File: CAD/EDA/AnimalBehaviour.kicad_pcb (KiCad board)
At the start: 2 copper layers, 106 x 86 mm, 26 parts, among them J1 SSR_INPUT, J10 Cam, J11 Imaging, J12 JSolenoid, J13 StimIsoIN, J2 SSR OUT, J3 StimCurrentInject, J4 StimIsoIN, J5 Imaging, J6 CAM, J7 AudioJack2, J8 Ext Supp, J9 LED, Q1 IRF540N, U1 4N35

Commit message: temp commit.
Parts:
- R1, R2, R3, R4: footprint Resistor_THT:R_Axial_DIN0414_L11.9mm_D4.5mm_P25.40mm_Horizontal -> Resistor_THT:R_Axial_DIN0309_L9.0mm_D3.2mm_P5.08mm_Vertical
- moved J7 81.4 mm to (115.6, 105.4), turned to 90 degrees
- moved J9 54.4 mm to (119.4, 92.7), turned to 90 degrees
- moved RotaryEncoder1 37.2 mm to (191.1, 102.9), turned to 270 degrees
- moved R2 33.3 mm to (148.0, 113.0), turned to 180 degrees
- moved R3 25.5 mm to (138.4, 113.0)
- moved J10 25.4 mm to (175.9, 63.5)
- moved J11 24.7 mm to (149.2, 62.9)
- moved Q1 23.1 mm to (152.4, 97.2), turned to 90 degrees
- moved R1 20.7 mm to (138.4, 106.7)
- moved J1 19.1 mm to (120.0, 77.5), turned to 270 degrees
- moved R4 17.1 mm to (117.5, 97.2)
- moved J8 14.1 mm to (116.2, 132.7)
- moved J12 12.9 mm to (116.8, 118.7)
- moved C1 8.78 mm to (172.7, 111.2)
- moved U1 8.17 mm to (164.5, 112.4)
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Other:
- net class Default: clearance 0.4 -> 0.25
- rule trace_clearance: 0.4 -> 0.25

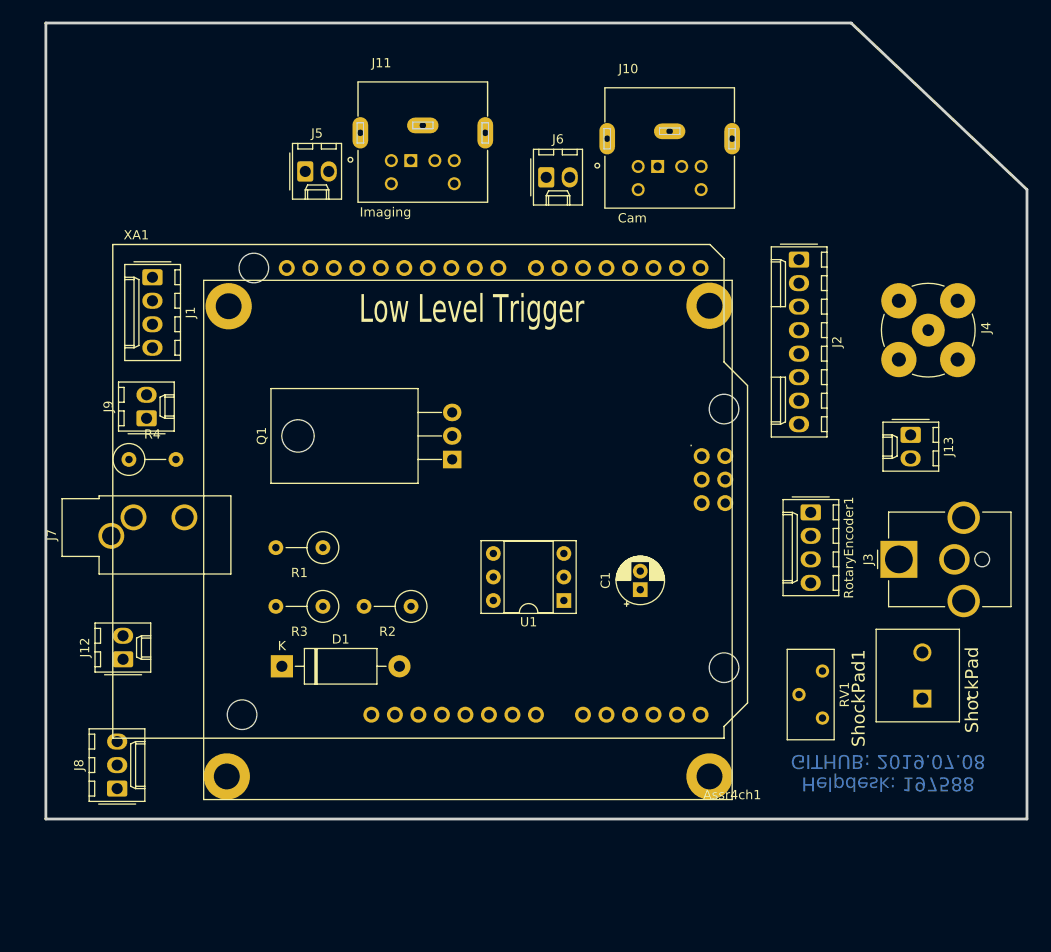
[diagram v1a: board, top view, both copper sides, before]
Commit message: Layout is autocomputed.
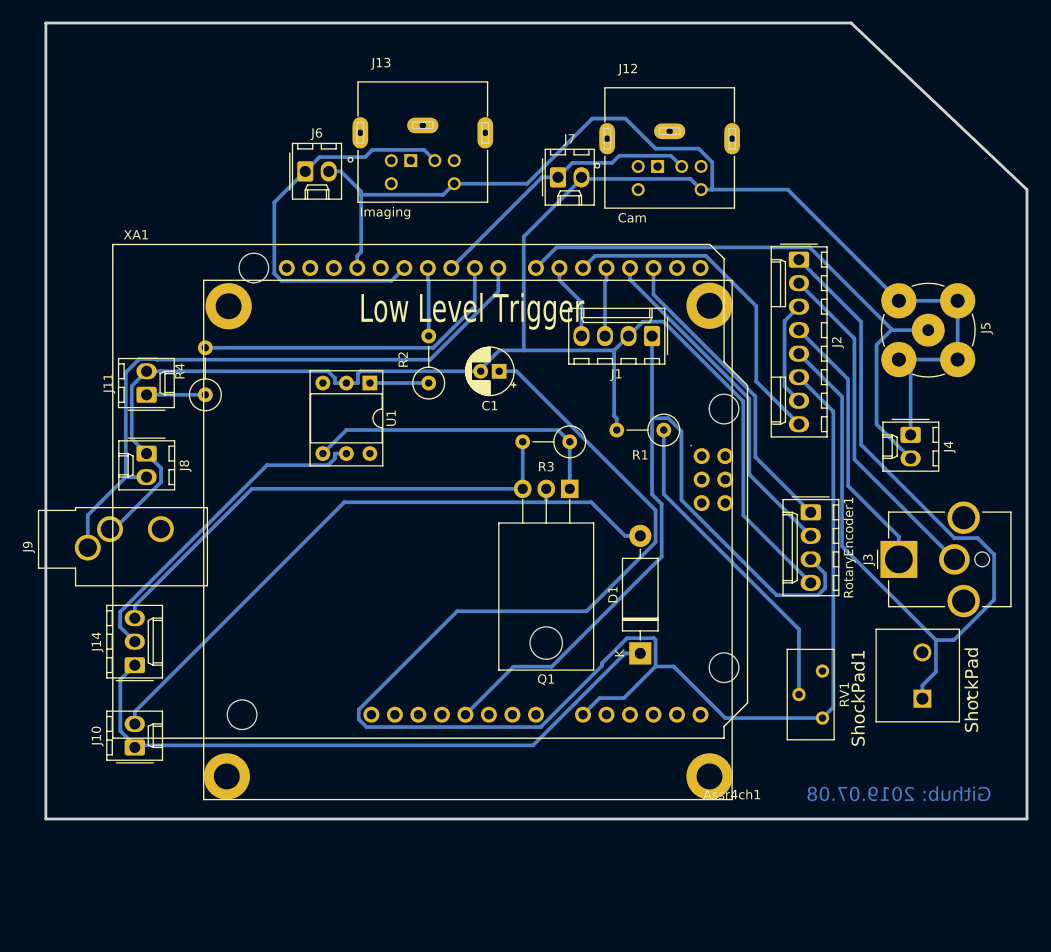
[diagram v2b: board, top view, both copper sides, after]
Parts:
- removed the J12 at (116.8, 118.7)
- added J10: JSolenoid, Connector_Molex:Molex_KK-254_AE-6410-02A_1x02_P2.54mm_Vertical, F.Cu at (118.1, 128.3)
- added J14: Ext Supp, Connector_Molex:Molex_KK-254_AE-6410-03A_1x03_P2.54mm_Vertical, F.Cu at (118.1, 119.4)
- J8: value Ext Supp -> TONE; footprint Connector_Molex:Molex_KK-254_AE-6410-03A_1x03_P2.54mm_Vertical -> Connector_Molex:Molex_KK-254_AE-6410-02A_1x02_P2.54mm_Vertical
- J9: renamed from J7; value AudioJack2 -> TONE
- moved J1 54.3 mm to (174.0, 83.8), turned to 180 degrees
- moved R1 39.0 mm to (175.3, 94.0)
- moved D1 38.7 mm to (172.7, 118.1), turned to 90 degrees
- moved J8 36.3 mm to (119.4, 96.5), turned to 270 degrees
- moved R3 32.1 mm to (165.1, 95.2)
- moved U1 31.5 mm to (143.5, 88.9), turned to 270 degrees
- moved C1 28.1 mm to (157.5, 87.6), turned to 180 degrees
- moved R2 24.2 mm to (149.9, 88.9), turned to 90 degrees
- moved Q1 13.1 mm to (165.1, 100.3), turned to 180 degrees
- moved R4 10.8 mm to (125.7, 90.2), turned to 90 degrees
- moved J9 2.84 mm to (113.0, 106.7)
- moved J11 2.54 mm to (119.4, 90.2)
- moved J7 1.27 mm to (163.8, 66.7)
- renumbered J9 to J11, J10 to J12, J11 to J13, J13 to J4, J4 to J5, J5 to J6, J6 to J7
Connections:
- J12 pad 1: (no net) -> Net-(J12-Pad1)
- J12 pad 3: (no net) -> Net-(J12-Pad3)
- J12 pad 4: (no net) -> Net-(J12-Pad4)
- J12 pad 5: (no net) -> Net-(J12-Pad5)
- J13 pad 1: (no net) -> Net-(J13-Pad1)
- J13 pad 3: (no net) -> Net-(J13-Pad3)
- J13 pad 4: (no net) -> Net-(J13-Pad4)
- J13 pad 5: (no net) -> Net-(J13-Pad5)
- J8 pad 1: EX_12V -> DGND
- J8 pad 2: EX_5V -> TONE+
- J9 pad T: AGND -> DGND
- RV1 pad 3: (no net) -> Net-(RV1-Pad3)
- U1 pad 3: (no net) -> Net-(U1-Pad3)
- U1 pad 6: (no net) -> Net-(U1-Pad6)
- XA1 pad 3V3: (no net) -> Net-(XA1-Pad3V3)
- XA1 pad 5V2: (no net) -> Net-(XA1-Pad5V2)
- XA1 pad A1: (no net) -> Net-(XA1-PadA1)
- XA1 pad A2: (no net) -> Net-(XA1-PadA2)
- XA1 pad A3: (no net) -> Net-(XA1-PadA3)
- XA1 pad A4: (no net) -> Net-(XA1-PadA4)
- XA1 pad A5: (no net) -> Net-(XA1-PadA5)
- XA1 pad AREF: (no net) -> Net-(XA1-PadAREF)
- XA1 pad D0: (no net) -> Net-(XA1-PadD0)
- XA1 pad D1: (no net) -> Net-(XA1-PadD1)
- XA1 pad D13: (no net) -> Net-(XA1-PadD13)
- XA1 pad GND2: (no net) -> Net-(XA1-PadGND2)
- XA1 pad GND3: (no net) -> Net-(XA1-PadGND3)
- XA1 pad GND4: (no net) -> Net-(XA1-PadGND4)
- XA1 pad IORF: (no net) -> Net-(XA1-PadIORF)
- XA1 pad MISO: (no net) -> Net-(XA1-PadMISO)
- XA1 pad MOSI: (no net) -> Net-(XA1-PadMOSI)
- XA1 pad RST1: (no net) -> Net-(XA1-PadRST1)
- XA1 pad RST2: (no net) -> Net-(XA1-PadRST2)
- XA1 pad SCK: (no net) -> Net-(XA1-PadSCK)
- XA1 pad SCL: (no net) -> Net-(XA1-PadSCL)
- XA1 pad SDA: (no net) -> Net-(XA1-PadSDA)
- XA1 pad VIN: (no net) -> Net-(XA1-PadVIN)
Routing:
- net DGND: track 0.00 -> 272.6 mm
- net ShockRead: track 0.00 -> 175.9 mm
- net PAD-: track 0.00 -> 99.0 mm
- net 5V: track 0.00 -> 87.6 mm
- net TONE+: track 0.00 -> 69.3 mm
- net EX_12V: track 0.00 -> 68.9 mm
- net Net-(D1-Pad2): track 0.00 -> 68.3 mm
- net ShockStimIsolator: track 0.00 -> 63.1 mm
- net AGND: track 0.00 -> 53.5 mm
- net ImagingTrig: track 0.00 -> 42.8 mm
- net EncB: track 0.00 -> 37.1 mm
- net OUT-: track 0.00 -> 36.8 mm
- net ShockPWM: track 0.00 -> 36.2 mm
- net EX_5V: track 0.00 -> 35.7 mm
- net LED: track 0.00 -> 35.1 mm
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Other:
- board text added: "Github: 2019.07.08"
- board text removed: "Helpdesk: 197588 GITHUB: 2019.07.08"

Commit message: layout was success.
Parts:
- moved J6 61.3 mm to (190.0, 96.0), turned to 270 degrees
- moved J13 57.9 mm to (204.2, 81.0), turned to 270 degrees
- moved ShockPad1 47.9 mm to (157.5, 137.5), turned to 0 degrees
- moved J7 44.0 mm to (190.0, 102.0), turned to 270 degrees
- moved J12 43.7 mm to (204.0, 97.0), turned to 270 degrees
- moved J2 40.4 mm to (190.0, 116.0)
- moved J5 29.8 mm to (203.0, 113.0)
- moved RV1 25.3 mm to (172.0, 140.0), turned to 180 degrees
- moved Q1 24.6 mm to (142.5, 110.0), turned to 270 degrees
- moved J3 21.1 mm to (200.0, 129.0)
- moved RotaryEncoder1 17.9 mm to (190.0, 85.0), turned to 90 degrees
- moved J4 12.8 mm to (190.0, 90.0)
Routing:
- net DGND: track 272.6 -> 0.00 mm
- net 5V: track 87.6 -> 275.2 mm
- net CamTTL: track 30.4 -> 126.4 mm
- net ShockRead: track 175.9 -> 94.9 mm
- net ShockPWM: track 36.2 -> 79.7 mm
- net ImagingTrig: track 42.8 -> 77.1 mm
- net Net-(Q1-Pad1): track 33.3 -> 54.8 mm
- net OUT+: track 29.2 -> 12.2 mm
- net OUT-: track 36.8 -> 20.3 mm
- net Puff: track 7.39 -> 22.6 mm
- net EncB: track 37.1 -> 22.0 mm
- net Net-(R1-Pad1): track 34.6 -> 48.2 mm
- net EncA: track 33.4 -> 20.7 mm
- net TONE+: track 69.3 -> 59.4 mm
- net ShockStimIsolator: track 63.1 -> 68.8 mm
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- added copper zone on B.Cu, net DGND
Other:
- board size 106 x 86 mm -> 105 x 72.5 mm

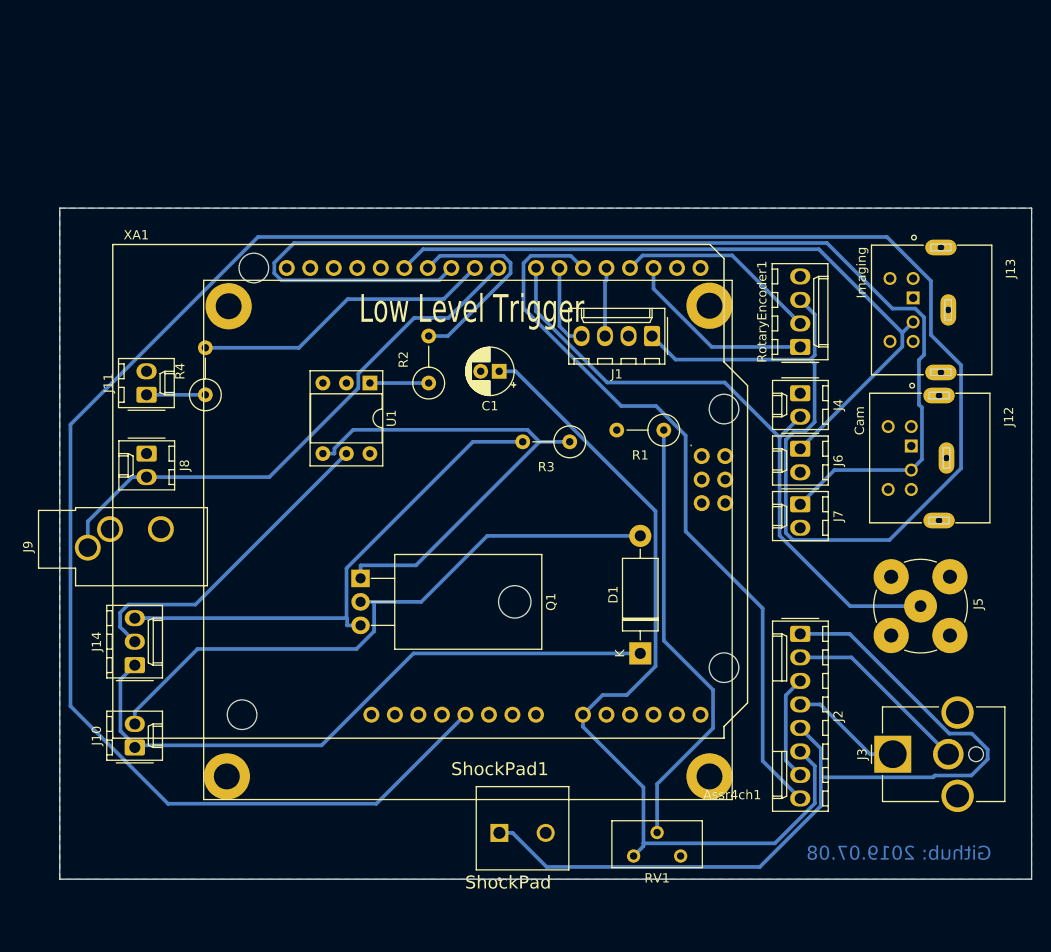
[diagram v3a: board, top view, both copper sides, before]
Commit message: Rearragenment of components. Shock related components on the bottom edge.
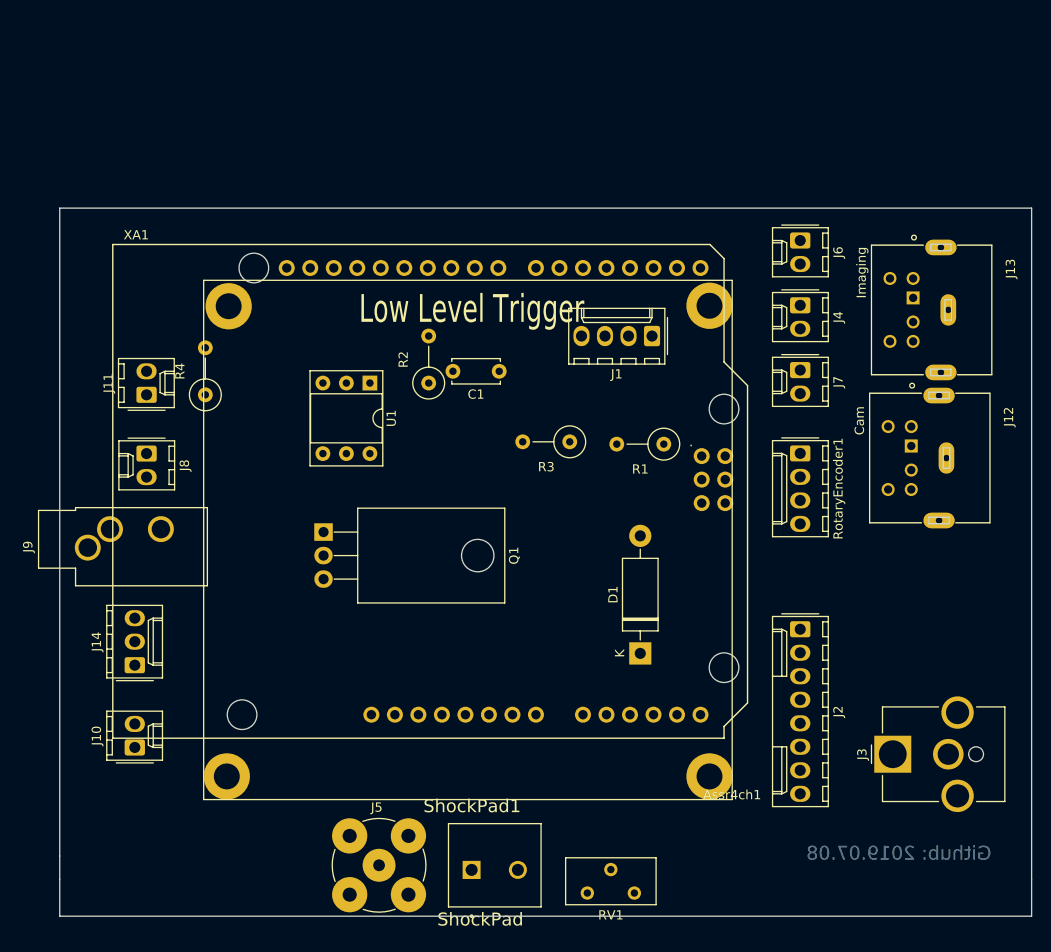
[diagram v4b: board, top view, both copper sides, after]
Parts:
- C1: footprint Capacitor_THT:CP_Radial_D5.0mm_P2.00mm -> Capacitor_THT:C_Disc_D5.0mm_W2.5mm_P5.00mm
- moved J5 64.9 mm to (144.5, 141.0), turned to 0 degrees
- moved J6 22.5 mm to (190.0, 73.5)
- moved J7 14.5 mm to (190.0, 87.5)
- moved RotaryEncoder1 11.5 mm to (190.0, 96.5), turned to 270 degrees
- moved J4 9.50 mm to (190.0, 80.5)
- moved Q1 6.40 mm to (138.5, 105.0)
- moved RV1 6.40 mm to (167.0, 144.0)
- moved ShockPad1 5.00 mm to (154.5, 141.5)
- moved R1 1.52 mm to (175.3, 95.5)
- moved J2 0.50 mm to (190.0, 115.5)
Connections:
- J12 pad 1: Net-(J12-Pad1) -> (no net)
- J12 pad 3: Net-(J12-Pad3) -> (no net)
- J12 pad 4: Net-(J12-Pad4) -> (no net)
- J12 pad 5: Net-(J12-Pad5) -> (no net)
- J13 pad 1: Net-(J13-Pad1) -> (no net)
- J13 pad 3: Net-(J13-Pad3) -> (no net)
- J13 pad 4: Net-(J13-Pad4) -> (no net)
- J13 pad 5: Net-(J13-Pad5) -> (no net)
- RV1 pad 3: Net-(RV1-Pad3) -> (no net)
- U1 pad 3: Net-(U1-Pad3) -> (no net)
- U1 pad 6: Net-(U1-Pad6) -> (no net)
- XA1 pad 3V3: Net-(XA1-Pad3V3) -> (no net)
- XA1 pad 5V2: Net-(XA1-Pad5V2) -> (no net)
- XA1 pad A1: Net-(XA1-PadA1) -> (no net)
- XA1 pad A2: Net-(XA1-PadA2) -> (no net)
- XA1 pad A3: Net-(XA1-PadA3) -> (no net)
- XA1 pad A4: Net-(XA1-PadA4) -> (no net)
- XA1 pad A5: Net-(XA1-PadA5) -> (no net)
- XA1 pad AREF: Net-(XA1-PadAREF) -> (no net)
- XA1 pad D0: Net-(XA1-PadD0) -> (no net)
- XA1 pad D1: Net-(XA1-PadD1) -> (no net)
- XA1 pad D13: Net-(XA1-PadD13) -> (no net)
- XA1 pad GND2: Net-(XA1-PadGND2) -> (no net)
- XA1 pad GND3: Net-(XA1-PadGND3) -> (no net)
- XA1 pad GND4: Net-(XA1-PadGND4) -> (no net)
- XA1 pad IORF: Net-(XA1-PadIORF) -> (no net)
- XA1 pad MISO: Net-(XA1-PadMISO) -> (no net)
- XA1 pad MOSI: Net-(XA1-PadMOSI) -> (no net)
- XA1 pad RST1: Net-(XA1-PadRST1) -> (no net)
- XA1 pad RST2: Net-(XA1-PadRST2) -> (no net)
- XA1 pad SCK: Net-(XA1-PadSCK) -> (no net)
- XA1 pad SCL: Net-(XA1-PadSCL) -> (no net)
- XA1 pad SDA: Net-(XA1-PadSDA) -> (no net)
- XA1 pad VIN: Net-(XA1-PadVIN) -> (no net)
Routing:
- net 5V: track 275.2 -> 0.00 mm
- net CamTTL: track 126.4 -> 0.00 mm
- net ShockRead: track 94.9 -> 0.00 mm
- net PAD-: track 93.6 -> 0.00 mm
- net ShockPWM: track 79.7 -> 0.00 mm
- net ImagingTrig: track 77.1 -> 0.00 mm
- net EX_12V: track 68.9 -> 0.00 mm
- net ShockStimIsolator: track 68.8 -> 0.00 mm
- net Net-(D1-Pad2): track 67.1 -> 0.00 mm
- net TONE+: track 59.4 -> 0.00 mm
- net AGND: track 55.2 -> 0.00 mm
- net Net-(Q1-Pad1): track 54.8 -> 0.00 mm
- net Net-(R1-Pad1): track 48.2 -> 0.00 mm
- net EX_5V: track 35.4 -> 0.00 mm
- net LED: track 32.7 -> 0.00 mm
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- removed copper zone on B.Cu, net DGND
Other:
- board size 105 x 72.5 mm -> 105 x 76.5 mm
